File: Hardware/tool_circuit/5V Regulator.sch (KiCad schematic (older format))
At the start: 5 parts

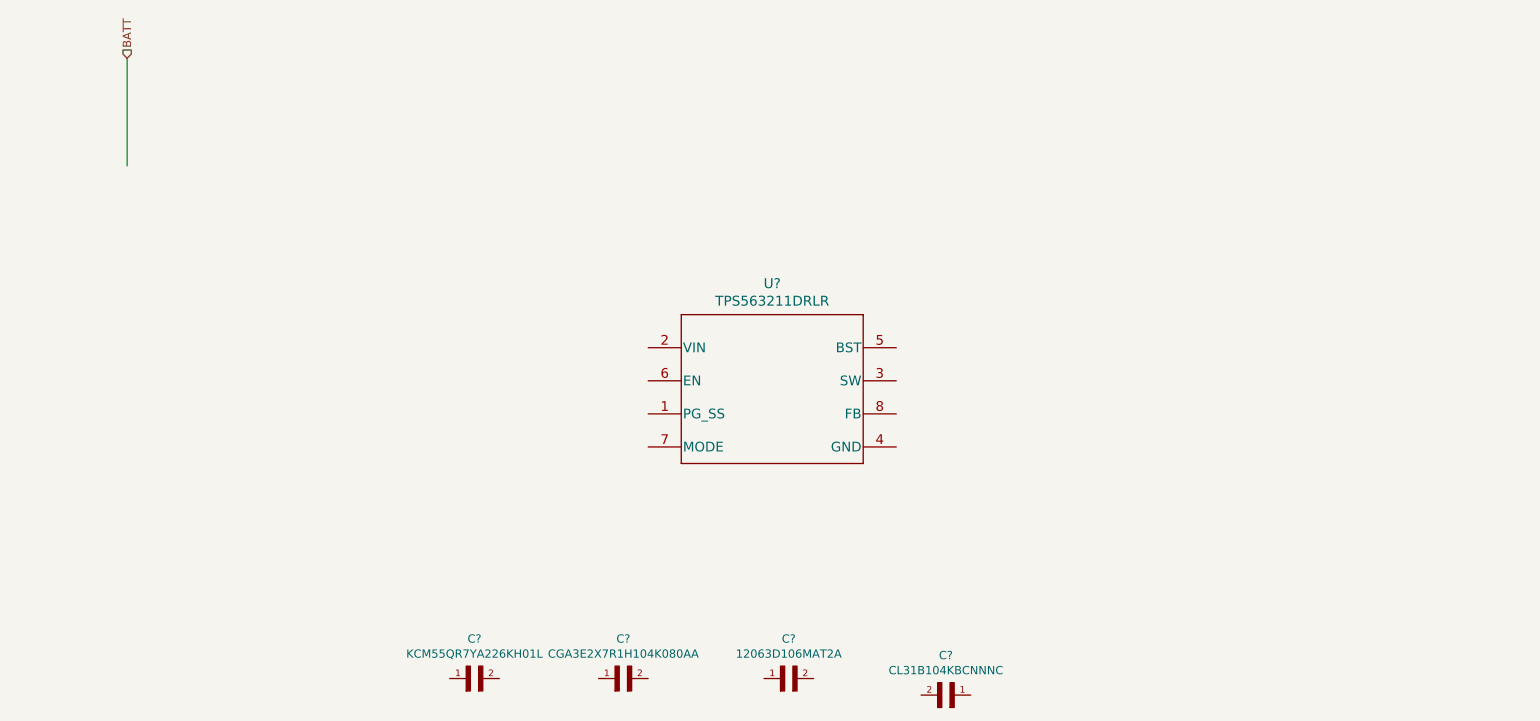
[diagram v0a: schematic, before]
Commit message: 5v regulator
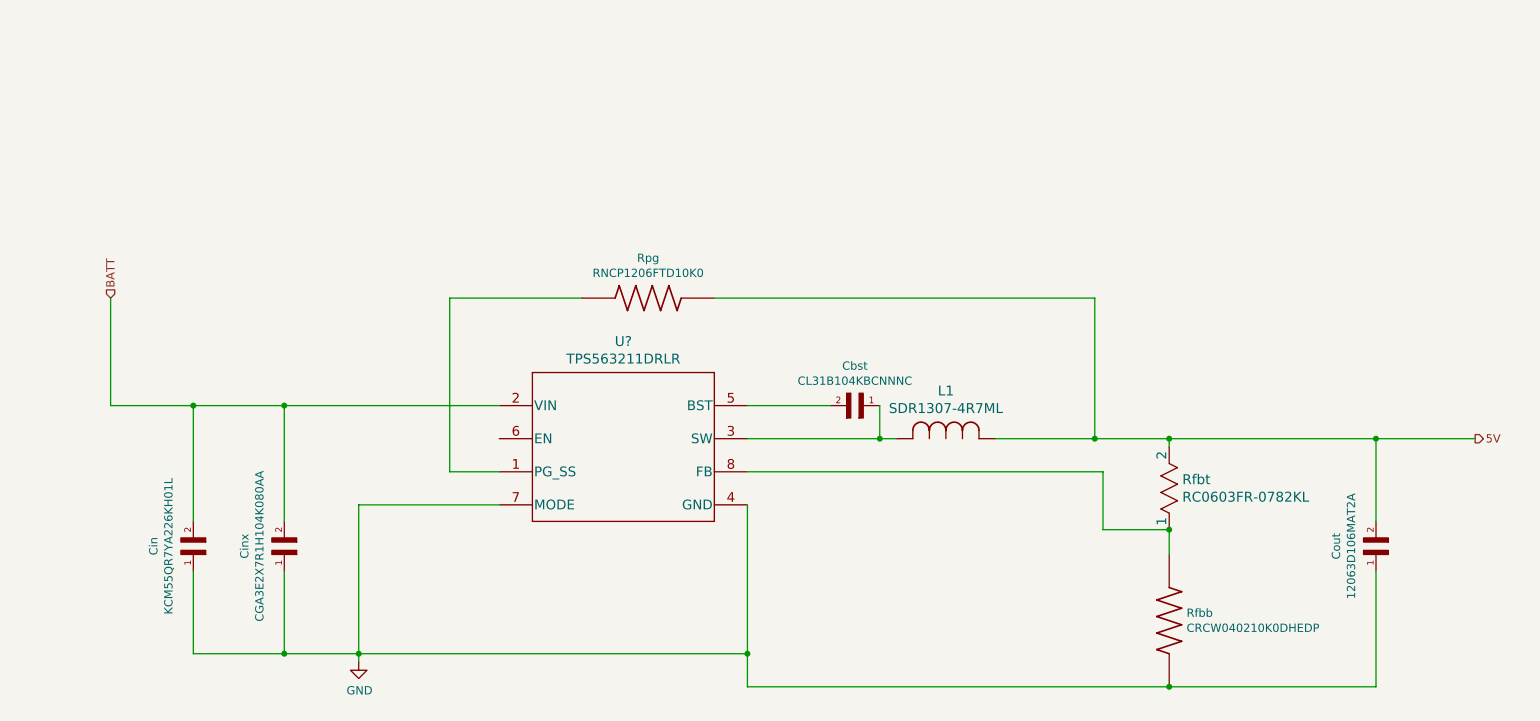
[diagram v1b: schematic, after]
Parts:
- added L1: SDR1307-4R7ML, IND_BOURNS_SDR1307, symbol 2021-09-13_22-06-51:SDR1307-4R7ML
- added Rfbb: CRCW040210K0DHEDP, RESC1005X40N, symbol CRCW040210K0DHEDP:CRCW040210K0DHEDP
- added Rfbt: RC0603FR-0782KL, RC0603N_YAG, symbol 2021-09-13_22-27-50:RC0603FR-0782KL
- added Rpg: RNCP1206FTD10K0, RESC3115X60N, symbol RNCP1206FTD10K0:RNCP1206FTD10K0
- gave numbers to parts that had none: 4
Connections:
- net labels added: 5V, GND
- wire segments 1 -> 38
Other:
- moved on the sheet: Cbst, Cin, Cinx, Cout, U?
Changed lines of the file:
@@
 Comment4 ""
 $EndDescr
-Text HLabel 2050 1400 1    50   Input ~ 0
+Text HLabel 1950 2850 1    50   Input ~ 0
 BATT
 Wire Wire Line
-	2050 1400 2050 2050
-$Comp
-L KCM55QR7YA226KH01L:KCM55QR7YA226KH01L C?
+	1950 2850 1950 3500
+$Comp
+L KCM55QR7YA226KH01L:KCM55QR7YA226KH01L Cin
 U 1 1 61326360
-P 4100 5150
-F 0 "C?" H 4150 5390 50  0000 C CNN
-F 1 "KCM55QR7YA226KH01L" H 4150 5299 50  0000 C CNN
-F 2 "CAPC6153X390N" H 4100 5150 50  0001 L BNN
-F 3 "https://www.snapeda.com/parts/KCM55QR7YA226KH01L/Murata%20Electronics/view-part/1365129/?welcome=home&ref=search&t=KCM55QR7YA226KH01L#" H 4100 5150 50  0001 L BNN
-	1    4100 5150
-	1    0    0    -1
-$EndComp
-$Comp
-L CGA3E2X7R1H104K080AA:CGA3E2X7R1H104K080AA C?
+P 2450 4400
+F 0 "Cin" H 2500 4640 50  0000 C CNN
+F 1 "KCM55QR7YA226KH01L" H 2500 4549 50  0000 C CNN
+F 2 "CAPC6153X390N" H 2450 4400 50  0001 L BNN
+F 3 "https://www.snapeda.com/parts/KCM55QR7YA226KH01L/Murata%20Electronics/view-part/1365129/?welcome=home&ref=search&t=KCM55QR7YA226KH01L#" H 2450 4400 50  0001 L BNN
+	1    2450 4400
+	0    -1   -1   0
+$EndComp
+$Comp
+L CGA3E2X7R1H104K080AA:CGA3E2X7R1H104K080AA Cinx
 U 1 1 61326D86
-P 5000 5150
-F 0 "C?" H 5050 5390 50  0000 C CNN
-F 1 "CGA3E2X7R1H104K080AA" H 5050 5299 50  0000 C CNN
-F 2 "CAPC1608X90N" H 5000 5150 50  0001 L BNN
-F 3 "" H 5000 5150 50  0001 L BNN
-	1    5000 5150
-	1    0    0    -1
-$EndComp
-$Comp
-L 12063D106MAT2A:12063D106MAT2A C?
+P 3000 4400
+F 0 "Cinx" H 3050 4640 50  0000 C CNN
+F 1 "CGA3E2X7R1H104K080AA" H 3050 4549 50  0000 C CNN
+F 2 "CAPC1608X90N" H 3000 4400 50  0001 L BNN
+F 3 "" H 3000 4400 50  0001 L BNN
+	1    3000 4400
+	0    -1   -1   0
+$EndComp
+$Comp
+L 12063D106MAT2A:12063D106MAT2A Cout
 U 1 1 613292F8
-P 6000 5150
-F 0 "C?" H 6050 5390 50  0000 C CNN
-F 1 "12063D106MAT2A" H 6050 5299 50  0000 C CNN
-F 2 "CAPC3216X178N" H 6000 5150 50  0001 L BNN
-F 3 "" H 6000 5150 50  0001 L BNN
-	1    6000 5150
-	1    0    0    -1
-$EndComp
-$Comp
-L CL31B104KBCNNNC:CL31B104KBCNNNC C?
+P 9600 4400
+F 0 "Cout" H 9650 4640 50  0000 C CNN
+F 1 "12063D106MAT2A" H 9650 4549 50  0000 C CNN
+F 2 "CAPC3216X178N" H 9600 4400 50  0001 L BNN
+F 3 "" H 9600 4400 50  0001 L BNN
+	1    9600 4400
+	0    -1   -1   0
+$EndComp
+$Comp
+L CL31B104KBCNNNC:CL31B104KBCNNNC Cbst
 U 1 1 6138E334
-P 6950 5250
-F 0 "C?" H 7000 5490 50  0000 C CNN
-F 1 "CL31B104KBCNNNC" H 7000 5399 50  0000 C CNN
-F 2 "CAPC3216X180N" H 6950 5250 50  0001 L BNN
-F 3 "" H 6950 5250 50  0001 L BNN
-	1    6950 5250
+P 6400 3500
+F 0 "Cbst" H 6450 3740 50  0000 C CNN
+F 1 "CL31B104KBCNNNC" H 6450 3649 50  0000 C CNN
+F 2 "CAPC3216X180N" H 6400 3500 50  0001 L BNN
+F 3 "" H 6400 3500 50  0001 L BNN
+	1    6400 3500
 	1    0    0    -1
 $EndComp
@@
 L TPS563211DRLR:TPS563211DRLR U?
 U 1 1 61393280
-P 5200 3150
-F 0 "U?" H 5950 3538 60  0000 C CNN
-F 1 "TPS563211DRLR" H 5950 3432 60  0000 C CNN
-F 2 "DRL0008A-MFG" H 5200 3090 60  0001 C CNN
-F 3 "" H 5200 3150 60  0000 C CNN
-	1    5200 3150
-	1    0    0    -1
-$EndComp
+P 4300 3500
+F 0 "U?" H 5050 3888 60  0000 C CNN
+F 1 "TPS563211DRLR" H 5050 3782 60  0000 C CNN
+F 2 "DRL0008A-MFG" H 4300 3440 60  0001 C CNN
+F 3 "" H 4300 3500 60  0000 C CNN
+	1    4300 3500
+	1    0    0    -1
+$EndComp
+Wire Wire Line
+	1950 3500 2450 3500
+Wire Wire Line
+	2450 4200 2450 3500
+Connection ~ 2450 3500
+Wire Wire Line
+	2450 3500 3000 3500
+Wire Wire Line
+	3000 4200 3000 3500
+Connection ~ 3000 3500
+Wire Wire Line
+	3000 3500 4300 3500
+$Comp
+L power:GND #PWR?
+U 1 1 61401F04
+P 3450 5050
+F 0 "#PWR?" H 3450 4800 50  0001 C CNN
+F 1 "GND" H 3455 4877 50  0000 C CNN
+F 2 "" H 3450 5050 50  0001 C CNN
+F 3 "" H 3450 5050 50  0001 C CNN
+	1    3450 5050
+	1    0    0    -1
+$EndComp
+Wire Wire Line
+	3000 4500 3000 5000
+Wire Wire Line
+	3000 5000 3450 5000
+Wire Wire Line
+	3450 5000 3450 5050
+Wire Wire Line
+	2450 4500 2450 5000
+Wire Wire Line
+	2450 5000 3000 5000
+Connection ~ 3000 5000
+Wire Wire Line
+	4300 4100 3450 4100
+Wire Wire Line
+	3450 4100 3450 5000
+Connection ~ 3450 5000
+Wire Wire Line
+	4300 3900 4000 3900
+Wire Wire Line
+	4000 3900 4000 2850
+Wire Wire Line
+	4000 2850 4800 2850
+$Comp
+L RNCP1206FTD10K0:RNCP1206FTD10K0 Rpg
+U 1 1 61403723
+P 5200 2850
+F 0 "Rpg" H 5200 3092 50  0000 C CNN
+F 1 "RNCP1206FTD10K0" H 5200 3001 50  0000 C CNN
+F 2 "RESC3115X60N" H 5200 2850 50  0001 L BNN
+F 3 "" H 5200 2850 50  0001 L BNN
+	1    5200 2850
+	1    0    0    -1
+$EndComp
+Wire Wire Line
+	5800 3500 6300 3500
+Wire Wire Line
+	5800 3700 6600 3700
+Wire Wire Line
+	6600 3700 6600 3500
+$Comp
+L 2021-09-13_22-06-51:SDR1307-4R7ML L1
+U 1 1 6140681E
+P 6700 3700
+F 0 "L1" H 7000 3989 60  0000 C CNN
+F 1 "SDR1307-4R7ML" H 7000 3883 60  0000 C CNN
+F 2 "IND_BOURNS_SDR1307" H 6975 3415 60  0001 C CNN
+F 3 "" H 6700 3700 60  0000 C CNN
+	1    6700 3700
+	1    0    0    -1
+$EndComp
+Wire Wire Line
+	6600 3700 6700 3700
+Connection ~ 6600 3700
+Wire Wire Line
+	5600 2850 7900 2850
+Wire Wire Line
+	7900 2850 7900 3700
+Wire Wire Line
+	7900 3700 7300 3700
+Wire Wire Line
+	5800 4100 5800 5000
+Wire Wire Line
+	5800 5000 3450 5000
+$Comp
+L 2021-09-13_22-27-50:RC0603FR-0782KL Rfbt
+U 1 1 6140CEA8
+P 8350 3750
+F 0 "Rfbt" V 8547 3829 60  0000 L CNN
+F 1 "RC0603FR-0782KL" V 8653 3829 60  0000 L CNN
+F 2 "RC0603N_YAG" H 8600 3415 60  0001 C CNN
+F 3 "" H 8350 3750 60  0000 C CNN
+	1    8350 3750
+	0    1    1    0
+$EndComp
+Wire Wire Line
+	7900 3700 8350 3700
+Wire Wire Line
+	8350 3700 8350 3750
+Connection ~ 7900 3700
+Wire Wire Line
+	5800 3900 7950 3900
+Wire Wire Line
+	7950 3900 7950 4250
+Wire Wire Line
+	7950 4250 8350 4250
+$Comp
+L CRCW040210K0DHEDP:CRCW040210K0DHEDP Rfbb
+U 1 1 6140F8A3
+P 8350 4800
+F 0 "Rfbb" V 8304 4905 50  0000 L CNN
+F 1 "CRCW040210K0DHEDP" V 8395 4905 50  0000 L CNN
+F 2 "RESC1005X40N" H 8350 4800 50  0001 L BNN
+F 3 "" H 8350 4800 50  0001 L BNN
+	1    8350 4800
+	0    1    1    0
+$EndComp
+Wire Wire Line
+	8350 4250 8350 4400
+Connection ~ 8350 4250
+Wire Wire Line
+	8350 5200 5800 5200
+Wire Wire Line
+	5800 5200 5800 5000
+Connection ~ 5800 5000
+Wire Wire Line
+	8350 3700 9600 3700
+Wire Wire Line
+	9600 3700 9600 4200
+Connection ~ 8350 3700
+Wire Wire Line
+	9600 4500 9600 5200
+Wire Wire Line
+	9600 5200 8350 5200
+Connection ~ 8350 5200
+Text HLabel 10200 3700 2    50   Output ~ 0
+5V
+Wire Wire Line
+	9600 3700 10200 3700
+Connection ~ 9600 3700
 $EndSCHEMATC

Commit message: symbols
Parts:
- Cbst1: renamed from Cbst; footprint CAPC3216X180N -> CL31B104KBCNNNC:CAPC3216X180N
- Cin1: renamed from Cin; footprint CAPC6153X390N -> KCM55QR7YA226KH01L:CAPC6153X390N
- Cinx1: renamed from Cinx; footprint CAPC1608X90N -> CGA3E2X7R1H104K080AA:CAPC1608X90N
- Cout1: renamed from Cout; footprint CAPC3216X178N -> 12063D106MAT2A:CAPC3216X178N
- Rfbb1: renamed from Rfbb; footprint RESC1005X40N -> CRCW040210K0DHEDP:RESC1005X40N
- Rpg1: renamed from Rpg; footprint RESC3115X60N -> RNCP1206FTD10K0:RESC3115X60N
- gave numbers to parts that had none: 1
- renumbered Rfbt to Rfbt1
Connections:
- net BATT renamed 12V_BATTERY
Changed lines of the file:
@@
 $Descr A4 11693 8268
 encoding utf-8
-Sheet 7 7
+Sheet 5 5
 Title ""
 Date ""
@@
 $EndDescr
 Text HLabel 1950 2850 1    50   Input ~ 0
-BATT
+12V_BATTERY
 Wire Wire Line
 	1950 2850 1950 3500
 $Comp
-L KCM55QR7YA226KH01L:KCM55QR7YA226KH01L Cin
+L KCM55QR7YA226KH01L:KCM55QR7YA226KH01L Cin1
 U 1 1 61326360
 P 2450 4400
-F 0 "Cin" H 2500 4640 50  0000 C CNN
+F 0 "Cin1" H 2500 4640 50  0000 C CNN
 F 1 "KCM55QR7YA226KH01L" H 2500 4549 50  0000 C CNN
-F 2 "CAPC6153X390N" H 2450 4400 50  0001 L BNN
+F 2 "KCM55QR7YA226KH01L:CAPC6153X390N" H 2450 4400 50  0001 L BNN
 F 3 "https://www.snapeda.com/parts/KCM55QR7YA226KH01L/Murata%20Electronics/view-part/1365129/?welcome=home&ref=search&t=KCM55QR7YA226KH01L#" H 2450 4400 50  0001 L BNN
 	1    2450 4400
@@
 $EndComp
 $Comp
-L CGA3E2X7R1H104K080AA:CGA3E2X7R1H104K080AA Cinx
+L CGA3E2X7R1H104K080AA:CGA3E2X7R1H104K080AA Cinx1
 U 1 1 61326D86
 P 3000 4400
-F 0 "Cinx" H 3050 4640 50  0000 C CNN
+F 0 "Cinx1" H 3050 4640 50  0000 C CNN
 F 1 "CGA3E2X7R1H104K080AA" H 3050 4549 50  0000 C CNN
-F 2 "CAPC1608X90N" H 3000 4400 50  0001 L BNN
+F 2 "CGA3E2X7R1H104K080AA:CAPC1608X90N" H 3000 4400 50  0001 L BNN
 F 3 "" H 3000 4400 50  0001 L BNN
 	1    3000 4400
@@
 $EndComp
 $Comp
-L 12063D106MAT2A:12063D106MAT2A Cout
+L 12063D106MAT2A:12063D106MAT2A Cout1
 U 1 1 613292F8
 P 9600 4400
-F 0 "Cout" H 9650 4640 50  0000 C CNN
+F 0 "Cout1" H 9650 4640 50  0000 C CNN
 F 1 "12063D106MAT2A" H 9650 4549 50  0000 C CNN
-F 2 "CAPC3216X178N" H 9600 4400 50  0001 L BNN
+F 2 "12063D106MAT2A:CAPC3216X178N" H 9600 4400 50  0001 L BNN
 F 3 "" H 9600 4400 50  0001 L BNN
 	1    9600 4400
@@
 $EndComp
 $Comp
-L CL31B104KBCNNNC:CL31B104KBCNNNC Cbst
+L CL31B104KBCNNNC:CL31B104KBCNNNC Cbst1
 U 1 1 6138E334
 P 6400 3500
-F 0 "Cbst" H 6450 3740 50  0000 C CNN
+F 0 "Cbst1" H 6450 3740 50  0000 C CNN
 F 1 "CL31B104KBCNNNC" H 6450 3649 50  0000 C CNN
-F 2 "CAPC3216X180N" H 6400 3500 50  0001 L BNN
+F 2 "CL31B104KBCNNNC:CAPC3216X180N" H 6400 3500 50  0001 L BNN
 F 3 "" H 6400 3500 50  0001 L BNN
 	1    6400 3500
@@
 $EndComp
 $Comp
-L TPS563211DRLR:TPS563211DRLR U?
+L TPS563211DRLR:TPS563211DRLR U4
 U 1 1 61393280
 P 4300 3500
-F 0 "U?" H 5050 3888 60  0000 C CNN
+F 0 "U4" H 5050 3888 60  0000 C CNN
 F 1 "TPS563211DRLR" H 5050 3782 60  0000 C CNN
 F 2 "DRL0008A-MFG" H 4300 3440 60  0001 C CNN
@@
 	3000 3500 4300 3500
 $Comp
-L power:GND #PWR?
+L power:GND #PWR0107
 U 1 1 61401F04
 P 3450 5050
-F 0 "#PWR?" H 3450 4800 50  0001 C CNN
+F 0 "#PWR0107" H 3450 4800 50  0001 C CNN
 F 1 "GND" H 3455 4877 50  0000 C CNN
 F 2 "" H 3450 5050 50  0001 C CNN
@@
 	4000 2850 4800 2850
 $Comp
-L RNCP1206FTD10K0:RNCP1206FTD10K0 Rpg
+L RNCP1206FTD10K0:RNCP1206FTD10K0 Rpg1
 U 1 1 61403723
 P 5200 2850
-F 0 "Rpg" H 5200 3092 50  0000 C CNN
+F 0 "Rpg1" H 5200 3092 50  0000 C CNN
 F 1 "RNCP1206FTD10K0" H 5200 3001 50  0000 C CNN
-F 2 "RESC3115X60N" H 5200 2850 50  0001 L BNN
+F 2 "RNCP1206FTD10K0:RESC3115X60N" H 5200 2850 50  0001 L BNN
 F 3 "" H 5200 2850 50  0001 L BNN
 	1    5200 2850
@@
 	5800 5000 3450 5000
 $Comp
-L 2021-09-13_22-27-50:RC0603FR-0782KL Rfbt
+L 2021-09-13_22-27-50:RC0603FR-0782KL Rfbt1
 U 1 1 6140CEA8
 P 8350 3750
-F 0 "Rfbt" V 8547 3829 60  0000 L CNN
+F 0 "Rfbt1" V 8547 3829 60  0000 L CNN
 F 1 "RC0603FR-0782KL" V 8653 3829 60  0000 L CNN
 F 2 "RC0603N_YAG" H 8600 3415 60  0001 C CNN
@@
 	7950 4250 8350 4250
 $Comp
-L CRCW040210K0DHEDP:CRCW040210K0DHEDP Rfbb
+L CRCW040210K0DHEDP:CRCW040210K0DHEDP Rfbb1
 U 1 1 6140F8A3
 P 8350 4800
-F 0 "Rfbb" V 8304 4905 50  0000 L CNN
+F 0 "Rfbb1" V 8304 4905 50  0000 L CNN
 F 1 "CRCW040210K0DHEDP" V 8395 4905 50  0000 L CNN
-F 2 "RESC1005X40N" H 8350 4800 50  0001 L BNN
+F 2 "CRCW040210K0DHEDP:RESC1005X40N" H 8350 4800 50  0001 L BNN
 F 3 "" H 8350 4800 50  0001 L BNN
 	1    8350 4800

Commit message: updated symbols/footprint paths for today
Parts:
- L1: footprint IND_BOURNS_SDR1307 -> ul_SDR1307-4R7ML:SDR1307-4R7ML
- R3: renamed from Rfbt1; footprint RC0603N_YAG -> ul_RC0603FR-0782KL:RC0603FR-0782KL
- U2: renamed from U4; footprint DRL0008A-MFG -> ul_TPS563211DRLR:TPS563211DRLR
- renumbered Cin1 to C1, Cinx1 to C2, Cbst1 to C3, Cout1 to C4, Rpg1 to R2, Rfbb1 to R4
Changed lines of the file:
@@
 $Descr A4 11693 8268
 encoding utf-8
-Sheet 5 5
+Sheet 4 5
 Title ""
 Date ""
@@
 	1950 2850 1950 3500
 $Comp
-L KCM55QR7YA226KH01L:KCM55QR7YA226KH01L Cin1
+L KCM55QR7YA226KH01L:KCM55QR7YA226KH01L C1
 U 1 1 61326360
 P 2450 4400
-F 0 "Cin1" H 2500 4640 50  0000 C CNN
+F 0 "C1" H 2500 4640 50  0000 C CNN
 F 1 "KCM55QR7YA226KH01L" H 2500 4549 50  0000 C CNN
 F 2 "KCM55QR7YA226KH01L:CAPC6153X390N" H 2450 4400 50  0001 L BNN
@@
 $EndComp
 $Comp
-L CGA3E2X7R1H104K080AA:CGA3E2X7R1H104K080AA Cinx1
+L CGA3E2X7R1H104K080AA:CGA3E2X7R1H104K080AA C2
 U 1 1 61326D86
 P 3000 4400
-F 0 "Cinx1" H 3050 4640 50  0000 C CNN
+F 0 "C2" H 3050 4640 50  0000 C CNN
 F 1 "CGA3E2X7R1H104K080AA" H 3050 4549 50  0000 C CNN
 F 2 "CGA3E2X7R1H104K080AA:CAPC1608X90N" H 3000 4400 50  0001 L BNN
@@
 $EndComp
 $Comp
-L 12063D106MAT2A:12063D106MAT2A Cout1
+L 12063D106MAT2A:12063D106MAT2A C4
 U 1 1 613292F8
 P 9600 4400
-F 0 "Cout1" H 9650 4640 50  0000 C CNN
+F 0 "C4" H 9650 4640 50  0000 C CNN
 F 1 "12063D106MAT2A" H 9650 4549 50  0000 C CNN
 F 2 "12063D106MAT2A:CAPC3216X178N" H 9600 4400 50  0001 L BNN
@@
 $EndComp
 $Comp
-L CL31B104KBCNNNC:CL31B104KBCNNNC Cbst1
+L CL31B104KBCNNNC:CL31B104KBCNNNC C3
 U 1 1 6138E334
 P 6400 3500
-F 0 "Cbst1" H 6450 3740 50  0000 C CNN
+F 0 "C3" H 6450 3740 50  0000 C CNN
 F 1 "CL31B104KBCNNNC" H 6450 3649 50  0000 C CNN
 F 2 "CL31B104KBCNNNC:CAPC3216X180N" H 6400 3500 50  0001 L BNN
@@
 $EndComp
 $Comp
-L TPS563211DRLR:TPS563211DRLR U4
+L TPS563211DRLR:TPS563211DRLR U2
 U 1 1 61393280
 P 4300 3500
-F 0 "U4" H 5050 3888 60  0000 C CNN
+F 0 "U2" H 5050 3888 60  0000 C CNN
 F 1 "TPS563211DRLR" H 5050 3782 60  0000 C CNN
-F 2 "DRL0008A-MFG" H 4300 3440 60  0001 C CNN
+F 2 "ul_TPS563211DRLR:TPS563211DRLR" H 4300 3440 60  0001 C CNN
 F 3 "" H 4300 3500 60  0000 C CNN
 	1    4300 3500
@@
 	4000 2850 4800 2850
 $Comp
-L RNCP1206FTD10K0:RNCP1206FTD10K0 Rpg1
+L RNCP1206FTD10K0:RNCP1206FTD10K0 R2
 U 1 1 61403723
 P 5200 2850
-F 0 "Rpg1" H 5200 3092 50  0000 C CNN
+F 0 "R2" H 5200 3092 50  0000 C CNN
 F 1 "RNCP1206FTD10K0" H 5200 3001 50  0000 C CNN
 F 2 "RNCP1206FTD10K0:RESC3115X60N" H 5200 2850 50  0001 L BNN
@@
 F 0 "L1" H 7000 3989 60  0000 C CNN
 F 1 "SDR1307-4R7ML" H 7000 3883 60  0000 C CNN
-F 2 "IND_BOURNS_SDR1307" H 6975 3415 60  0001 C CNN
+F 2 "ul_SDR1307-4R7ML:SDR1307-4R7ML" H 6975 3415 60  0001 C CNN
 F 3 "" H 6700 3700 60  0000 C CNN
 	1    6700 3700
@@
 	5800 5000 3450 5000
 $Comp
-L 2021-09-13_22-27-50:RC0603FR-0782KL Rfbt1
+L 2021-09-13_22-27-50:RC0603FR-0782KL R3
 U 1 1 6140CEA8
 P 8350 3750
-F 0 "Rfbt1" V 8547 3829 60  0000 L CNN
+F 0 "R3" V 8547 3829 60  0000 L CNN
 F 1 "RC0603FR-0782KL" V 8653 3829 60  0000 L CNN
-F 2 "RC0603N_YAG" H 8600 3415 60  0001 C CNN
+F 2 "ul_RC0603FR-0782KL:RC0603FR-0782KL" H 8600 3415 60  0001 C CNN
 F 3 "" H 8350 3750 60  0000 C CNN
 	1    8350 3750
@@
 	7950 4250 8350 4250
 $Comp
-L CRCW040210K0DHEDP:CRCW040210K0DHEDP Rfbb1
+L CRCW040210K0DHEDP:CRCW040210K0DHEDP R4
 U 1 1 6140F8A3
 P 8350 4800
-F 0 "Rfbb1" V 8304 4905 50  0000 L CNN
+F 0 "R4" V 8304 4905 50  0000 L CNN
 F 1 "CRCW040210K0DHEDP" V 8395 4905 50  0000 L CNN
 F 2 "CRCW040210K0DHEDP:RESC1005X40N" H 8350 4800 50  0001 L BNN
